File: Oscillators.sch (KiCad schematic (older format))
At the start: 7 parts

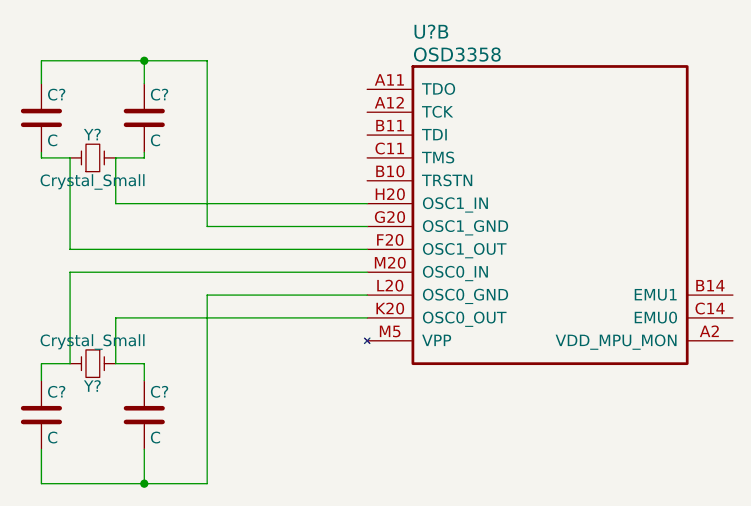
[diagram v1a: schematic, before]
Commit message: Added USB Host and Device
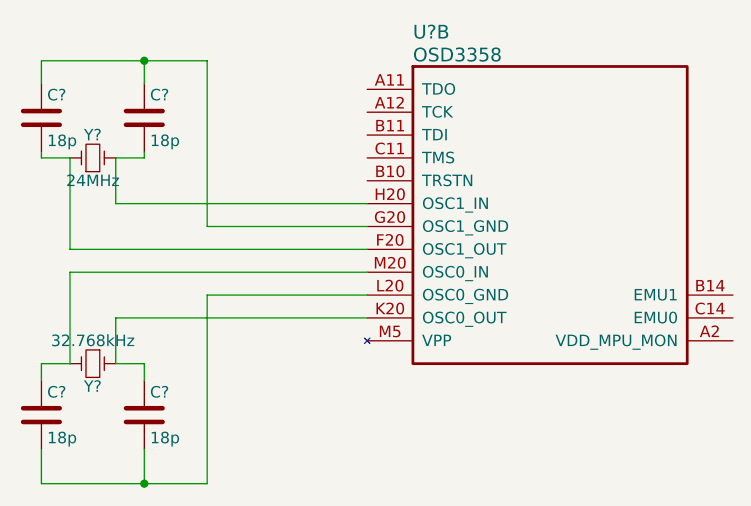
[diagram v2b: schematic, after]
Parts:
- C? (x4): value C -> 18p
- Y?: value Crystal_Small -> 24MHz
- Y?: value Crystal_Small -> 32.768kHz
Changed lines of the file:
@@
 P 3625 2825
 F 0 "Y?" H 3625 2925 50  0000 C CNN
-F 1 "Crystal_Small" H 3625 2725 50  0000 C CNN
+F 1 "24MHz" H 3625 2725 50  0000 C CNN
 F 2 "" H 3625 2825 50  0000 C CNN
 F 3 "" H 3625 2825 50  0000 C CNN
@@
 P 3625 3725
 F 0 "Y?" H 3625 3825 50  0000 C CNN
-F 1 "Crystal_Small" H 3625 3625 50  0000 C CNN
+F 1 "32.768kHz" H 3625 3625 50  0000 C CNN
 F 2 "" H 3625 3725 50  0000 C CNN
 F 3 "" H 3625 3725 50  0000 C CNN
@@
 P 3400 3950
 F 0 "C?" H 3425 4050 50  0000 L CNN
-F 1 "C" H 3425 3850 50  0000 L CNN
+F 1 "18p" H 3425 3850 50  0000 L CNN
 F 2 "" H 3438 3800 50  0000 C CNN
 F 3 "" H 3400 3950 50  0000 C CNN
@@
 P 3850 3950
 F 0 "C?" H 3875 4050 50  0000 L CNN
-F 1 "C" H 3875 3850 50  0000 L CNN
+F 1 "18p" H 3875 3850 50  0000 L CNN
 F 2 "" H 3888 3800 50  0000 C CNN
 F 3 "" H 3850 3950 50  0000 C CNN
@@
 P 3850 2650
 F 0 "C?" H 3875 2750 50  0000 L CNN
-F 1 "C" H 3875 2550 50  0000 L CNN
+F 1 "18p" H 3875 2550 50  0000 L CNN
 F 2 "" H 3888 2500 50  0000 C CNN
 F 3 "" H 3850 2650 50  0000 C CNN
@@
 P 3400 2650
 F 0 "C?" H 3425 2750 50  0000 L CNN
-F 1 "C" H 3425 2550 50  0000 L CNN
+F 1 "18p" H 3425 2550 50  0000 L CNN
 F 2 "" H 3438 2500 50  0000 C CNN
 F 3 "" H 3400 2650 50  0000 C CNN
